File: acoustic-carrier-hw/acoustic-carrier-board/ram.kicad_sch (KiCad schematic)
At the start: 28 parts, among them IC1 ECP5-BGA256, IC2 MT41K256M16TW-107_P

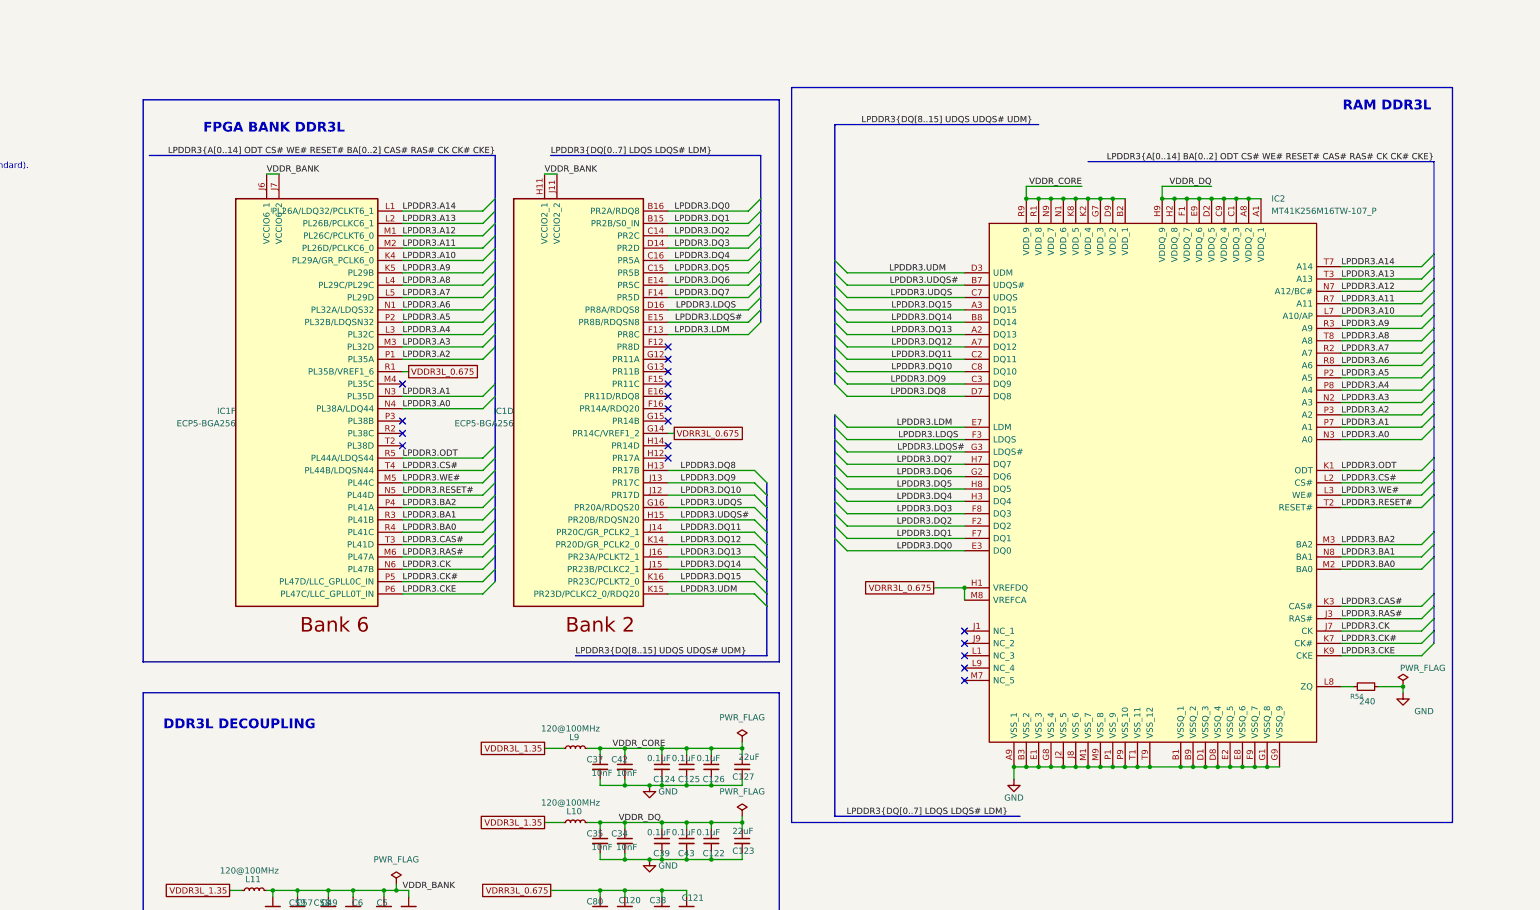
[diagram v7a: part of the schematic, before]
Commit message: [¢arrier] Fixed busses, added resistive arrays instead of 4x4k7 or 4x10k
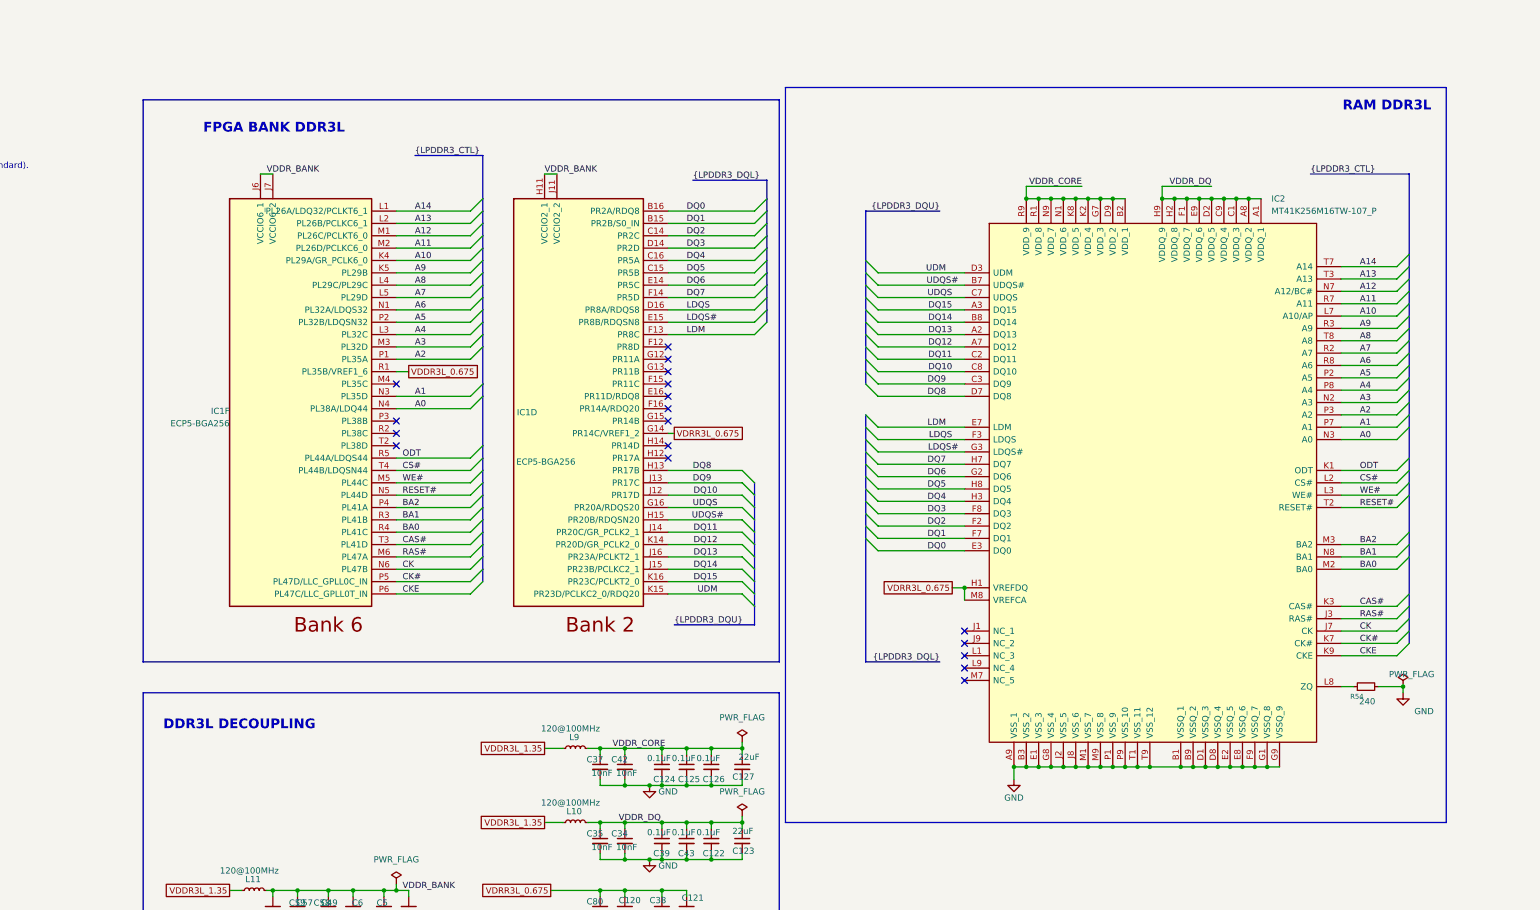
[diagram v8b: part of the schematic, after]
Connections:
- net LPDDR3.A0 renamed A0
- net LPDDR3.A1 renamed A1
- net LPDDR3.A10 renamed A10
- net LPDDR3.A11 renamed A11
- net LPDDR3.A12 renamed A12
- net LPDDR3.A13 renamed A13
- net LPDDR3.A14 renamed A14
- net LPDDR3.A2 renamed A2
- net LPDDR3.A3 renamed A3
- net LPDDR3.A4 renamed A4
- net LPDDR3.A5 renamed A5
- net LPDDR3.A6 renamed A6
- net LPDDR3.A7 renamed A7
- net LPDDR3.A8 renamed A8
- net LPDDR3.A9 renamed A9
- net LPDDR3.BA0 renamed BA0
- net LPDDR3.BA1 renamed BA1
- net LPDDR3.BA2 renamed BA2
- net LPDDR3.CAS# renamed CAS#
- net LPDDR3.CK renamed CK
- net LPDDR3.CK# renamed CK#
- net LPDDR3.CKE renamed CKE
- net LPDDR3.CS# renamed CS#
- net LPDDR3.DQ0 renamed DQ0
- net LPDDR3.DQ1 renamed DQ1
- net LPDDR3.DQ10 renamed DQ10
- net LPDDR3.DQ11 renamed DQ11
- net LPDDR3.DQ12 renamed DQ12
- net LPDDR3.DQ13 renamed DQ13
- net LPDDR3.DQ14 renamed DQ14
- net LPDDR3.DQ15 renamed DQ15
- net LPDDR3.DQ2 renamed DQ2
- net LPDDR3.DQ3 renamed DQ3
- net LPDDR3.DQ4 renamed DQ4
- net LPDDR3.DQ5 renamed DQ5
- net LPDDR3.DQ6 renamed DQ6
- net LPDDR3.DQ7 renamed DQ7
- net LPDDR3.DQ8 renamed DQ8
- net LPDDR3.DQ9 renamed DQ9
- net LPDDR3.LDM renamed LDM
- net LPDDR3.LDQS renamed LDQS
- net LPDDR3.LDQS# renamed LDQS#
- net LPDDR3.ODT renamed ODT
- net LPDDR3.RAS# renamed RAS#
- net LPDDR3.RESET# renamed RESET#
- net LPDDR3.UDM renamed UDM
- net LPDDR3.UDQS renamed UDQS
- net LPDDR3.UDQS# renamed UDQS#
- net LPDDR3.WE# renamed WE#
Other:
- moved on the sheet: IC1F
